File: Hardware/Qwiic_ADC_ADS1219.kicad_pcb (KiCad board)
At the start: 2 copper layers, 25.4 x 25.4 mm, 81 parts, among them J1 Qwiic_RA, J2 Qwiic_RA, J3 Conn_01x06, J4 Conn_01x06, J5 Conn_01x02, J6 I2C_01x04, U1 ADS1219IPW

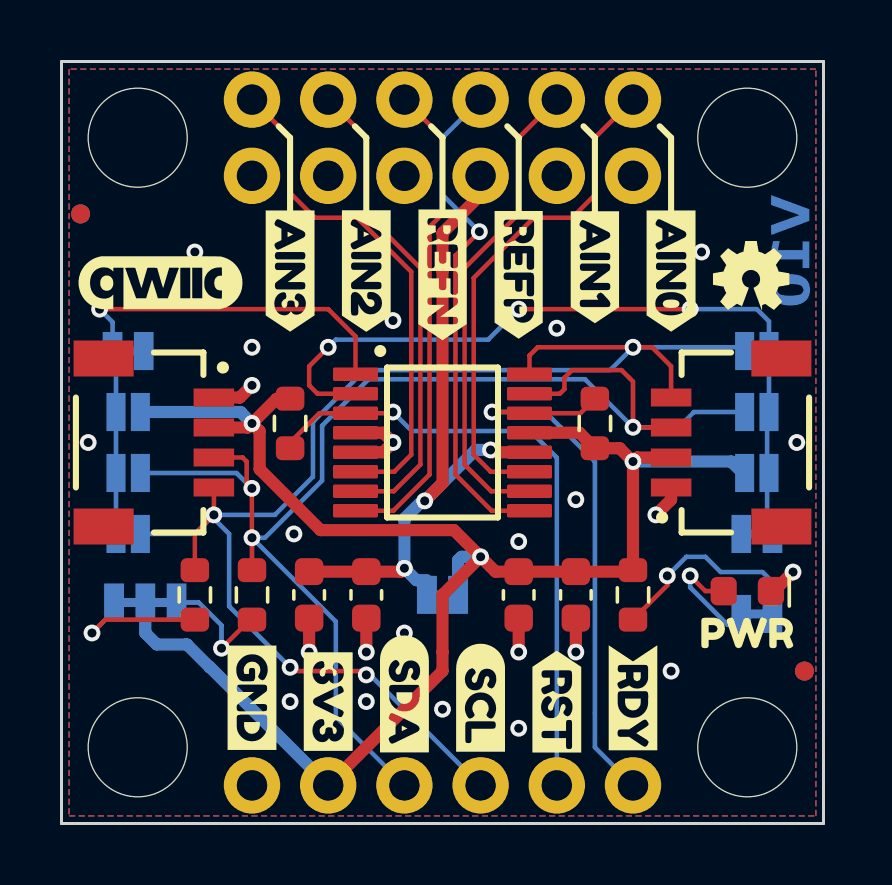
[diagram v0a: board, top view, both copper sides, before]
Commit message: Update silk. Change address jumper names.
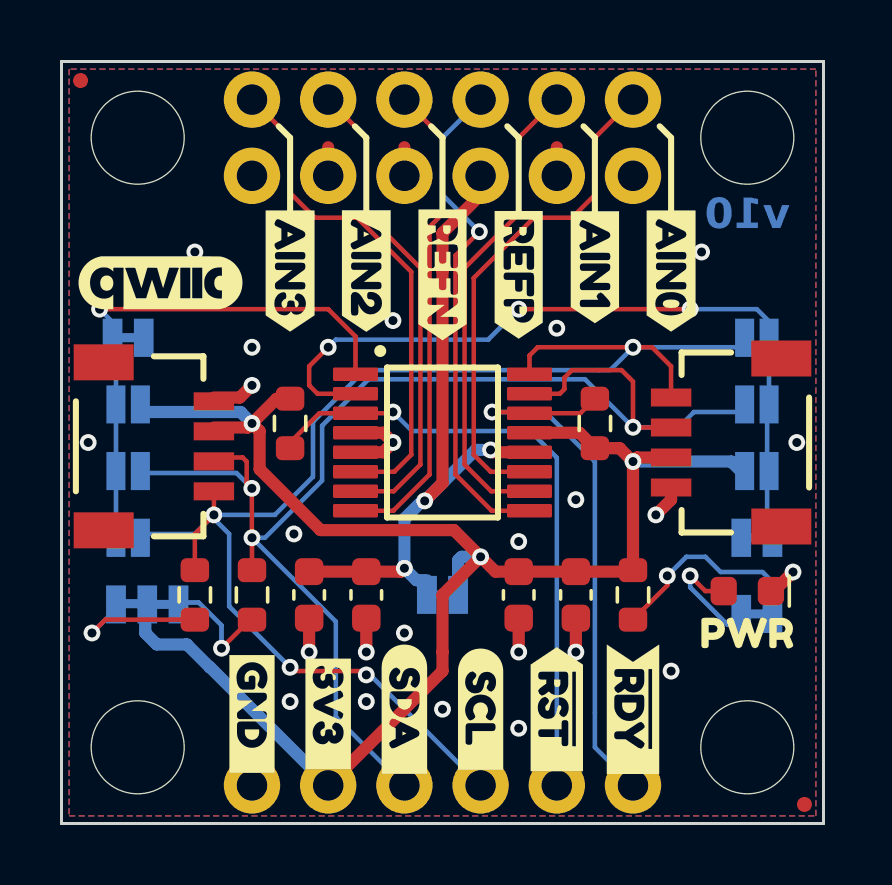
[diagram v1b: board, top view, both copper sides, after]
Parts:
- removed FID2, FID4: Fiducial_0.635, SparkFun-Aesthetic:Fiducial_0.635mm
- removed Ref**: Val**, SparkFun-Aesthetic:OSHW-LOGO-MINI
- removed U2: ~, SparkFun-Aesthetic:ORDERING_INSTRUCTIONS
- removed kibuzzard-64C36E7A (x7): G***, kibuzzard-64C36E7A
- removed kibuzzard-64C36EF5: G***, kibuzzard-64C36EF5
- removed kibuzzard-64C37519: G***, kibuzzard-64C37519
- removed kibuzzard-64C3756D: G***, kibuzzard-64C3756D
- removed kibuzzard-64C375B4: G***, kibuzzard-64C375B4
- removed kibuzzard-64C375BE: G***, kibuzzard-64C375BE
- removed kibuzzard-64C375C5: G***, kibuzzard-64C375C5
- removed kibuzzard-64C375DA: G***, kibuzzard-64C375DA
- removed kibuzzard-64C375F2: G***, kibuzzard-64C375F2
- removed kibuzzard-64C37614: G***, kibuzzard-64C37614
- removed kibuzzard-64C3761E: G***, kibuzzard-64C3761E
- removed the kibuzzard-64C37A88 at (135.9, 122.9) (x2)
- removed kibuzzard-64C37AD1: G***, kibuzzard-64C37AD1
- removed kibuzzard-64C37B05: G***, kibuzzard-64C37B05
- removed kibuzzard-64C37B2E: G***, kibuzzard-64C37B2E
- removed kibuzzard-64C37B4E: G***, kibuzzard-64C37B4E
- removed kibuzzard-64C37B97: G***, kibuzzard-64C37B97
- removed kibuzzard-64C37BC1: G***, kibuzzard-64C37BC1
- removed kibuzzard-64C37BF9: G***, kibuzzard-64C37BF9
- removed kibuzzard-64C37C16: G***, kibuzzard-64C37C16
- removed kibuzzard-64C37C5C: G***, kibuzzard-64C37C5C
- removed kibuzzard-64C37D63: G***, kibuzzard-64C37D63
- removed kibuzzard-64C37FAB: G***, kibuzzard-64C37FAB
- added kibuzzard-67BCC03F: G***, kibuzzard-67BCC03F, F.Cu at (133.3, 123.3)
- added kibuzzard-67BCE7E0: G***, kibuzzard-67BCE7E0, B.Cu at (131.6, 110.8)
- added kibuzzard-67BCE805: G***, kibuzzard-67BCE805, B.Cu at (131.6, 113.0)
- added kibuzzard-67BCE809: G***, kibuzzard-67BCE809, B.Cu at (131.4, 115.3)
- added kibuzzard-67BCE80E: G***, kibuzzard-67BCE80E, B.Cu at (131.4, 117.5)
- added kibuzzard-67BCE889: G***, kibuzzard-67BCE889, B.Cu at (147.8, 117.5)
- added kibuzzard-67BCE896: G***, kibuzzard-67BCE896, B.Cu at (148.0, 115.3)
- added kibuzzard-67BCE899: G***, kibuzzard-67BCE899, B.Cu at (148.0, 113.0)
- added kibuzzard-67BCE89D: G***, kibuzzard-67BCE89D, B.Cu at (148.0, 110.8)
- added kibuzzard-67BCE9A5: G***, kibuzzard-67BCE9A5, F.Cu at (143.5, 123.2)
- added kibuzzard-67BCE9C9: G***, kibuzzard-67BCE9C9, F.Cu at (138.4, 123.2)
- added kibuzzard-67BCE9CD: G***, kibuzzard-67BCE9CD, F.Cu at (141.0, 123.2)
- added kibuzzard-67BCE9E1: G***, kibuzzard-67BCE9E1, F.Cu at (135.9, 123.3)
- added kibuzzard-67BCEA1E: G***, kibuzzard-67BCEA1E, B.Cu at (143.5, 123.2)
- added kibuzzard-67BCEA31: G***, kibuzzard-67BCEA31, B.Cu at (141.0, 123.2)
- added kibuzzard-67BCEA3A: G***, kibuzzard-67BCEA3A, B.Cu at (138.4, 123.2)
- added kibuzzard-67BCEA48: G***, kibuzzard-67BCEA48, B.Cu at (135.9, 123.5)
- added kibuzzard-67BCEA55: G***, kibuzzard-67BCEA55, B.Cu at (133.3, 123.3)
- added kibuzzard-67BCEA65: G***, kibuzzard-67BCEA65, B.Cu at (146.1, 123.2)
- added kibuzzard-67BCEA70: G***, kibuzzard-67BCEA70, F.Cu at (146.1, 123.2)
- added kibuzzard-67BCEAAB: G***, kibuzzard-67BCEAAB, B.Cu at (147.0, 120.0)
- added kibuzzard-67BCEAC6: G***, kibuzzard-67BCEAC6, B.Cu at (143.5, 107.8)
- added kibuzzard-67BCEAC6: G***, kibuzzard-67BCEAC6, B.Cu at (133.3, 107.8)
- added kibuzzard-67BCEAC6: G***, kibuzzard-67BCEAC6, B.Cu at (138.4, 107.8)
- added kibuzzard-67BCEAC6: G***, kibuzzard-67BCEAC6, B.Cu at (135.9, 107.8)
- added kibuzzard-67BCEAC6: G***, kibuzzard-67BCEAC6, B.Cu at (146.1, 107.8)
- added kibuzzard-67BCEAE1: G***, kibuzzard-67BCEAE1, B.Cu at (141.0, 108.3)
- added kibuzzard-67BCEB15: G***, kibuzzard-67BCEB15, B.Cu at (129.2, 108.3)
- added kibuzzard-67BCEB1D: G***, kibuzzard-67BCEB1D, B.Cu at (150.2, 108.6)
- added kibuzzard-67BCEB32: G***, kibuzzard-67BCEB32, B.Cu at (139.7, 117.0)
- C2, C4: value 0.1uF_0603_25V_20% -> 0.1uF
- D1: footprint SparkFun-LED:LED_0603_1608Metric -> SparkFun-LED:LED_0603_1608Metric_Red
- FID1, FID3: value Fiducial_0.635 -> Fiducial_0.5mm; footprint SparkFun-Aesthetic:Fiducial_0.635mm -> SparkFun-Aesthetic:Fiducial_0.5mm_Mask1mm
- J1, J2: footprint SparkFun-Connector:JST04_1MM_RA -> SparkFun-Connector:JST_SMD_1.0mm-4_Black
- J3, J4: footprint SparkFun-Connector:1X06 -> SparkFun-Connector:1x06
- J5: footprint SparkFun-Connector:1X02 -> SparkFun-Connector:1x02
- J6: value I2C_01x04 -> I2C; footprint SparkFun-Connector:1X04 -> SparkFun-Connector:1x04
- JP1, JP2: footprint SparkFun-Jumper:SMT-JUMPER_2_NC_TRACE_SILK -> SparkFun-Jumper:Jumper_2_NC_Trace
- JP10, JP6: value ~ -> D; footprint SparkFun-Jumper:SMT-JUMPER_2_NO_SILK -> SparkFun-Jumper:Jumper_2_NO
- JP11, JP7: value ~ -> C; footprint SparkFun-Jumper:SMT-JUMPER_2_NO_SILK -> SparkFun-Jumper:Jumper_2_NO
- JP3: footprint SparkFun-Jumper:SMT-JUMPER_3_2-NC_TRACE_SILK -> SparkFun-Jumper:Jumper_3_NC-2_Trace
- JP4, JP8: value ~ -> G; footprint SparkFun-Jumper:SMT-JUMPER_2_NC_TRACE_SILK -> SparkFun-Jumper:Jumper_2_NC_Trace
- JP5, JP9: value ~ -> V; footprint SparkFun-Jumper:SMT-JUMPER_2_NO_SILK -> SparkFun-Jumper:Jumper_2_NO
- ST1, ST2, ST3, ST4: value Stand_off -> Standoff; footprint SparkFun-Hardware:STAND-OFF -> SparkFun-Hardware:Standoff
- moved FID3 4.45 mm to (127.6, 102.2)
- moved FID1 4.44 mm to (151.8, 126.4)
- moved JP11 0.44 mm to (150.2, 110.8)
- moved JP4 0.44 mm to (129.2, 110.8)
- moved JP10 0.25 mm to (150.2, 113.0)
- moved JP5 0.25 mm to (129.2, 113.0)
- moved kibuzzard-64C38090 0.19 mm to (129.8, 121.6)
- moved J1 0.13 mm to (132.1, 114.4)
- moved JP7 0.13 mm to (129.2, 117.5)
- moved JP8 0.13 mm to (150.2, 117.5)
- moved JP3 0.09 mm to (129.9, 119.7)
- moved JP6 0.06 mm to (129.2, 115.3)
- moved JP9 0.06 mm to (150.2, 115.3)
- turned R1 to 90 degrees
- turned R2 to -90 degrees
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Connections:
- C1 pad 1: +3.3V -> 3.3V
- C2 pad 1: +3.3V -> 3.3V
- J1 pad 2: +3.3V -> 3.3V
- J2 pad 2: +3.3V -> 3.3V
- J6 pad 2: +3.3V -> 3.3V
- JP1 pad 1: +3.3V -> 3.3V
- JP3 pad 2: +3.3V -> 3.3V
- JP3 pad 3: Net-(JP3-B) -> Net-(JP3-C)
- JP5 pad 2: +3.3V -> 3.3V
- JP9 pad 2: +3.3V -> 3.3V
- R1 pad 1: +3.3V -> Net-(JP2-B)
- R1 pad 2: Net-(JP2-B) -> 3.3V
- R2 pad 1: Net-(JP3-B) -> SCL
- R2 pad 2: SCL -> Net-(JP3-C)
- R4 pad 1: +3.3V -> ~{DRDY}
- R4 pad 2: ~{DRDY} -> 3.3V
- R5 pad 1: +3.3V -> 3.3V
- U1 pad 13: +3.3V -> 3.3V
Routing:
- net 3.3V: track 0.00 -> 54.9 mm, vias 0 -> 3
- net +3.3V: track 54.9 -> 0.00 mm, vias 3 -> 0
- net Net-(JP3-C): track 0.00 -> 4.93 mm, vias 0 -> 1
- net Net-(JP3-B): track 4.93 -> 0.00 mm, vias 1 -> 0
- net GND: track 10.8 -> 13.7 mm
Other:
- copper layers 2 -> 4
- rule pad_to_mask_clearance: 0 -> 0.05
- board text added: "Controlled Impedance: No"
- board text added: "Finish: Lead-Free HASL"
- board text added: "Layers: 2"
- board text added: "Material: TG135-140"
- board text added: "Ordering Notes"
- board text added: "Outer Copper Weight: 1oz"
- board text added: "Silkscreen Color: White"
- board text added: "Solder Mask: Red"
- board text added: "Thickness: 1.6mm"
- board text added: "v10"
- board text removed: "Solder Mask: Red Silkscreen: White Layers: 2 Finish: HASL Lead-free Thickness: 1.6mm Copper weight: 1oz"
- board text removed: "V10"

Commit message: Changes board setup to two layers and adds measures
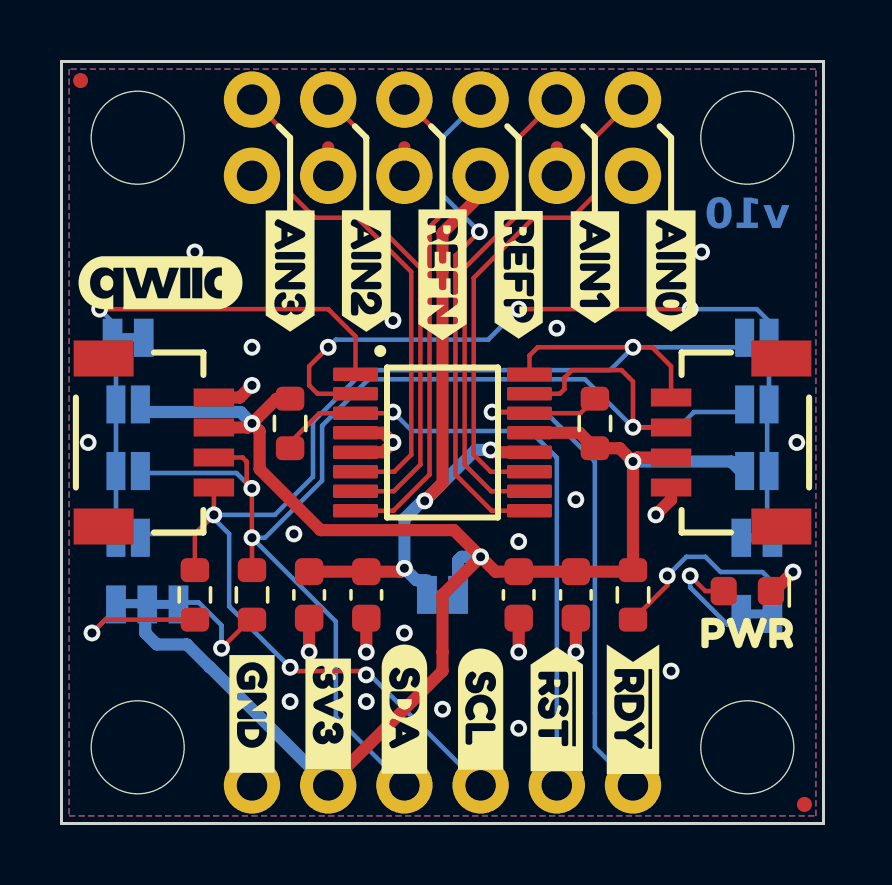
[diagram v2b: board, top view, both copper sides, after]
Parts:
- moved J1 0.13 mm to (132.1, 114.3)
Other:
- copper layers 4 -> 2
